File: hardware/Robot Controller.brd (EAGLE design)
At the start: 50.5 x 38.1 mm, 10 parts

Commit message: added a host pin
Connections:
- new net N$2: ATTINY.15, JP1.11
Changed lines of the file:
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@@
 <wire x1="81.2292" y1="76.2" x2="81.28" y2="76.2" width="0.254" layer="1"/>
+</signal>
+<signal name="N$2">
+<contactref element="JP1" pad="11"/>
+<contactref element="ATTINY" pad="15"/>
+<wire x1="71.755" y1="55.88" x2="81.28" y2="63.5" width="0" layer="19" extent="1-1"/>
 </signal>
 </signals>

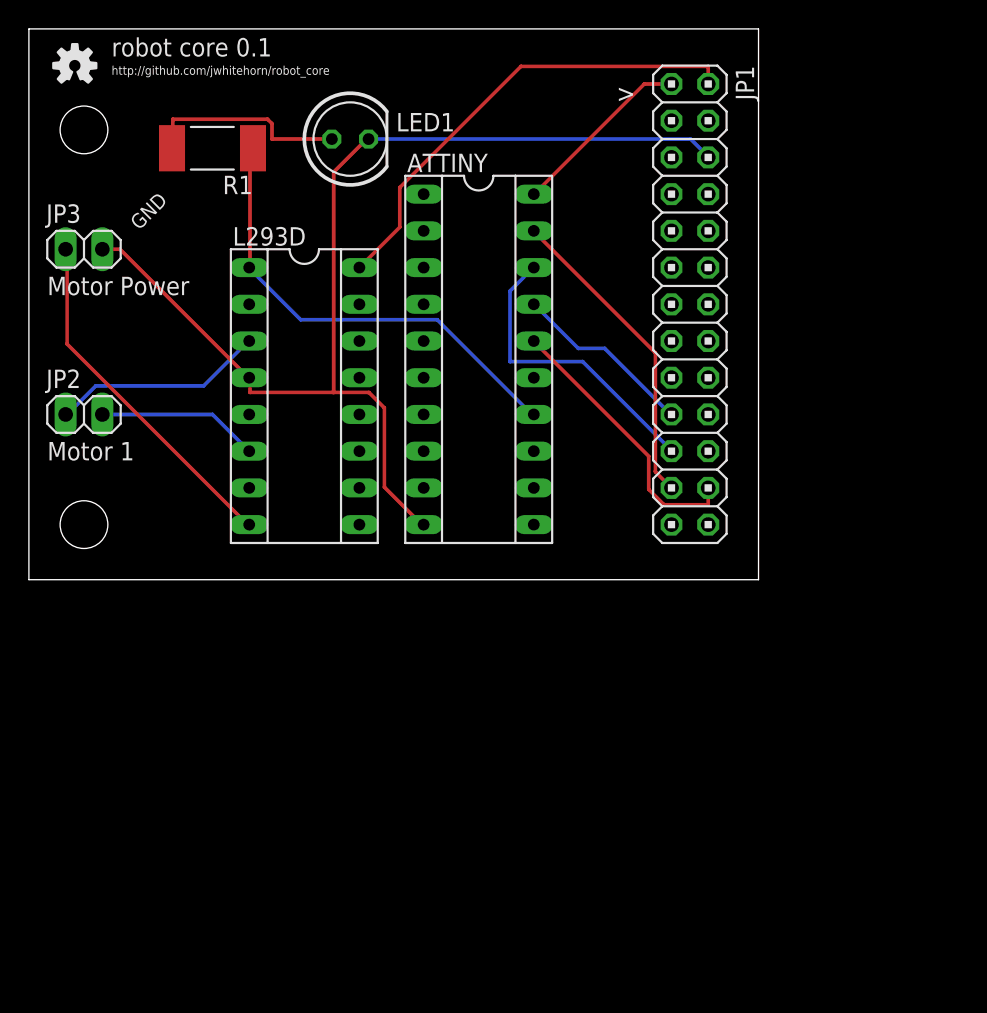
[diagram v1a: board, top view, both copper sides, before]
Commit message: thinking out how motor direction will be controlled
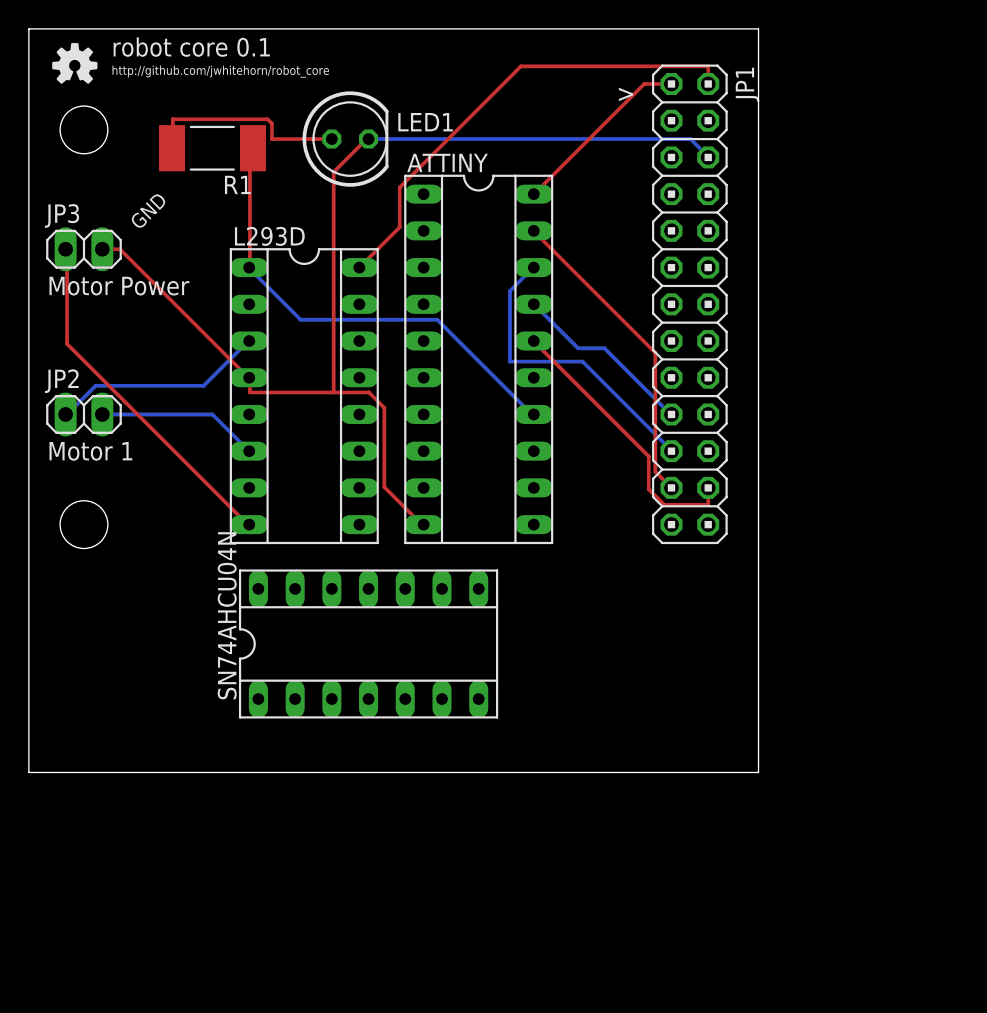
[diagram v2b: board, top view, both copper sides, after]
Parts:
- added SN74AHCU04N: (no value), ic-package:SOCKET-14
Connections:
- new net N$13: ATTINY.4, L293D.7, SN74AHCU04N.13
- new net N$15: L293D.2, SN74AHCU04N.12
- net GND: now also L293D.12, L293D.13, L293D.5, SN74AHCU04N.7
- net VCC: now also SN74AHCU04N.14
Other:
- board size 50.5 x 38.1 mm -> 50.5 x 51.4 mm
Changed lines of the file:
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@@
 <board>
 <plain>
-<wire x1="36.83" y1="41.91" x2="87.3" y2="41.91" width="0" layer="20"/>
-<wire x1="87.3" y1="41.91" x2="87.3" y2="80" width="0" layer="20"/>
-<wire x1="36.83" y1="80" x2="36.83" y2="41.91" width="0" layer="20"/>
+<wire x1="36.83" y1="28.575" x2="87.3" y2="28.575" width="0" layer="20"/>
+<wire x1="87.3" y1="28.575" x2="87.3" y2="80" width="0" layer="20"/>
+<wire x1="36.83" y1="80" x2="36.83" y2="28.575" width="0" layer="20"/>
 <text x="44.45" y="66.04" size="1.016" layer="21" rot="R45">GND</text>
 <text x="38.1" y="61.595" size="1.27" layer="21">Motor Power</text>
@@
 <element name="LED1" library="led" package="LED5MM" value="" x="59.055" y="72.39"/>
 <element name="U$4" library="SparkFun-Aesthetics" package="OSHW-LOGO-S" value="" x="40.005" y="77.47"/>
+<element name="SN74AHCU04N" library="ic-package" package="SOCKET-14" value="" x="60.325" y="37.465"/>
 </elements>
 <signals>
@@
 <wire x1="83.82" y1="71.1708" x2="83.82" y2="71.12" width="0.254" layer="16"/>
 <wire x1="60.3504" y1="72.39" x2="60.325" y2="72.39" width="0.254" layer="16"/>
+<contactref element="L293D" pad="13"/>
+<contactref element="L293D" pad="12"/>
+<contactref element="L293D" pad="5"/>
+<contactref element="SN74AHCU04N" pad="7"/>
+<wire x1="60.3504" y1="54.864" x2="59.69" y2="55.88" width="0" layer="19" extent="1-1"/>
+<wire x1="52.07" y1="53.34" x2="52.1208" y2="54.864" width="0" layer="19" extent="1-1"/>
+<wire x1="59.69" y1="53.34" x2="60.3504" y2="54.864" width="0" layer="19" extent="1-1"/>
+<wire x1="67.945" y1="33.655" x2="64.008" y2="45.72" width="0" layer="19" extent="1-1"/>
 </signal>
 <signal name="VCC">
@@
 <wire x1="71.7804" y1="68.58" x2="71.755" y2="68.58" width="0.254" layer="1"/>
 <wire x1="81.2292" y1="76.2" x2="81.28" y2="76.2" width="0.254" layer="1"/>
+<contactref element="SN74AHCU04N" pad="14"/>
+<wire x1="52.705" y1="41.275" x2="71.7804" y2="68.58" width="0" layer="19" extent="1-1"/>
 </signal>
 <signal name="N$2">
@@
 <wire x1="71.755" y1="55.88" x2="81.28" y2="63.5" width="0" layer="19" extent="1-1"/>
 </signal>
+<signal name="N$13">
+<contactref element="ATTINY" pad="4"/>
+<contactref element="SN74AHCU04N" pad="13"/>
+<contactref element="L293D" pad="7"/>
+<wire x1="52.07" y1="48.26" x2="64.135" y2="60.96" width="0" layer="19" extent="1-1"/>
+<wire x1="55.245" y1="41.275" x2="52.07" y2="48.26" width="0" layer="19" extent="1-1"/>
+</signal>
+<signal name="N$15">
+<contactref element="L293D" pad="2"/>
+<contactref element="SN74AHCU04N" pad="12"/>
+<wire x1="57.785" y1="41.275" x2="52.07" y2="60.96" width="0" layer="19" extent="1-1"/>
+</signal>
 </signals>

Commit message: tweak hardware design
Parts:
- removed JP2: Motor 1, pinhead:1X02
- removed JP3: Motor Power, pinhead:1X02
- removed U$1, U$2: (no value), SparkFun-Electromechanical:STAND-OFF
- removed U$4: (no value), SparkFun-Aesthetics:OSHW-LOGO-S
- added H1, H2: MOUNT-HOLE2.8, holes:2,8
- added LED2: (no value), led:1206
- added R2: (no value), resistor:R3216
- added SL1, SL2: (no value), con-amp-quick:02P
- LED1: device led:LED5MM -> led:1206
- R1: device resistor:R6332 -> resistor:R3216
- moved L293D 35.3 mm to (77.5, 26.7), turned to 0 degrees
- moved R1 31.0 mm to (74.9, 54.0), turned to 0 degrees
- moved LED1 28.5 mm to (85.7, 62.2), turned to 180 degrees
- moved JP1 18.4 mm to (95.9, 48.3)
- moved ATTINY 18.3 mm to (83.2, 47.0)
- moved SN74AHCU04N 12.8 mm to (71.8, 43.2), turned to 270 degrees
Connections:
- removed net N$11: LED1.A, R1.2
- new net N$16: ATTINY.2, R2.1
- new net N$17: LED2.A, R2.2
- new net N$3: LED1.A, R1.1
- net GND: now also LED1.C, LED2.C, SL2.2; no longer JP3.2, LED1.K
- net N$1: now also R1.2; no longer R1.1
- net N$10: now also SL2.1; no longer JP3.1
- net N$8: now also SL1.2; no longer JP2.1
- net N$9: now also SL1.1; no longer JP2.2
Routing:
- net N$10: track 24.4 -> 64.7 mm
- net N$8: track 14.8 -> 51.6 mm, vias 0 -> 1
- net N$13: track 0.00 -> 35.5 mm, vias 0 -> 1
- net N$9: track 11.2 -> 44.6 mm
- net GND: track 76.5 -> 108.7 mm
- net N$12: track 32.7 -> 58.3 mm
- net N$15: track 0.00 -> 24.8 mm
- net N$17: track 0.00 -> 23.7 mm
- net N$1: track 32.3 -> 52.1 mm, vias 0 -> 1
- net N$3: track 0.00 -> 17.5 mm, vias 0 -> 2
- net N$16: track 0.00 -> 17.0 mm
- net VCC: track 12.7 -> 28.1 mm
- net N$11: track 14.2 -> 0.00 mm
- net N$2: track 0.00 -> 9.79 mm
- net N$5: track 12.7 -> 18.1 mm
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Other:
- board size 50.5 x 51.4 mm -> 37.8 x 48.2 mm
- board text added: "robot core"
- board text removed: "GND"
- board text removed: "http://github.com/jwhitehorn/robot_core"
- board text removed: "robot core 0.1"

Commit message: change host pin
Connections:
- net N$2: now also ATTINY.3; no longer ATTINY.15
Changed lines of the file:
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@@
 <signal name="N$2">
 <contactref element="JP1" pad="11"/>
-<contactref element="ATTINY" pad="15"/>
 <wire x1="89.916" y1="48.6156" x2="87.0204" y2="45.72" width="0.254" layer="16"/>
 <wire x1="92.5068" y1="48.6156" x2="89.916" y2="48.6156" width="0.254" layer="16"/>
 <wire x1="94.6404" y1="50.7492" x2="92.5068" y2="48.6156" width="0.254" layer="16"/>
-<wire x1="87.0204" y1="45.72" x2="86.995" y2="45.72" width="0.254" layer="16"/>
 <wire x1="94.6404" y1="50.7492" x2="94.615" y2="50.8" width="0.254" layer="16"/>
+<contactref element="ATTINY" pad="3"/>
+<wire x1="79.375" y1="53.34" x2="87.0204" y2="45.72" width="0" layer="19" extent="16-16"/>
 </signal>
 <signal name="N$13">

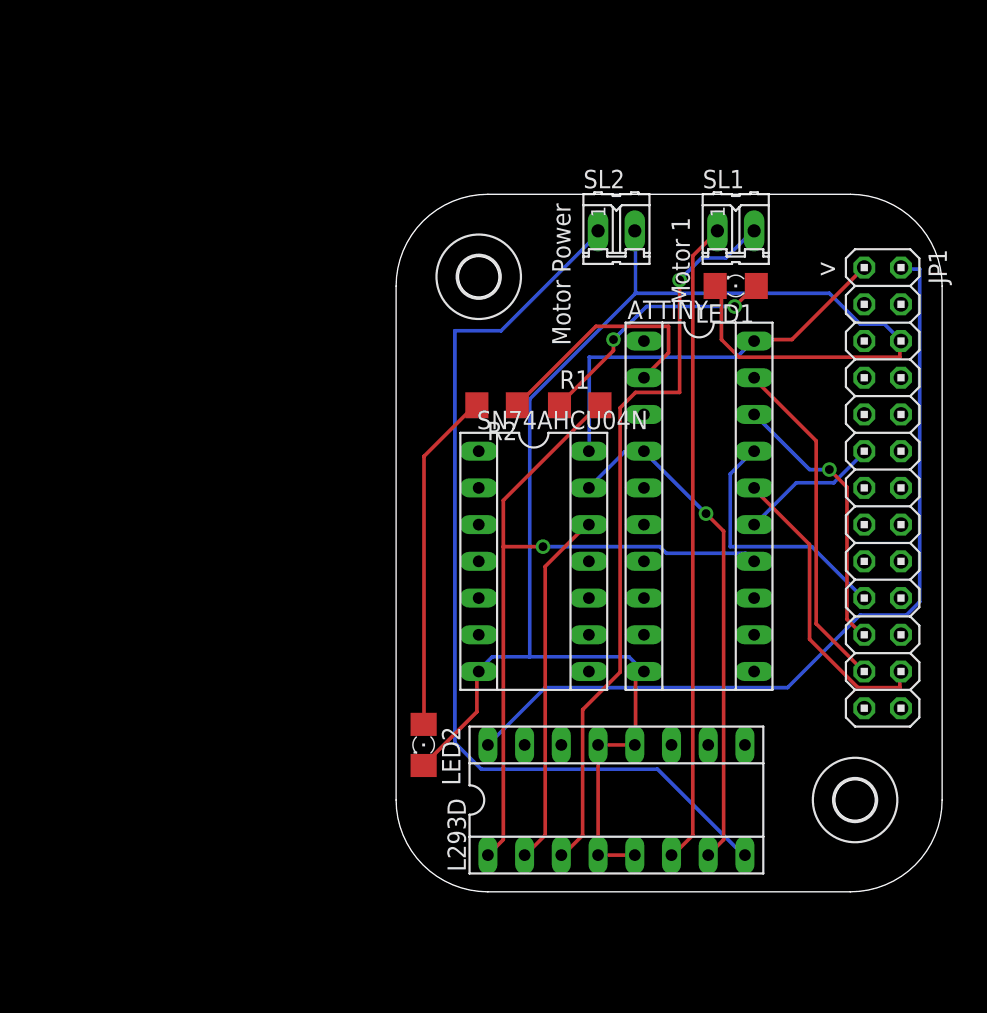
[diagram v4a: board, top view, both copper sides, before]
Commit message: update hardware for second motor
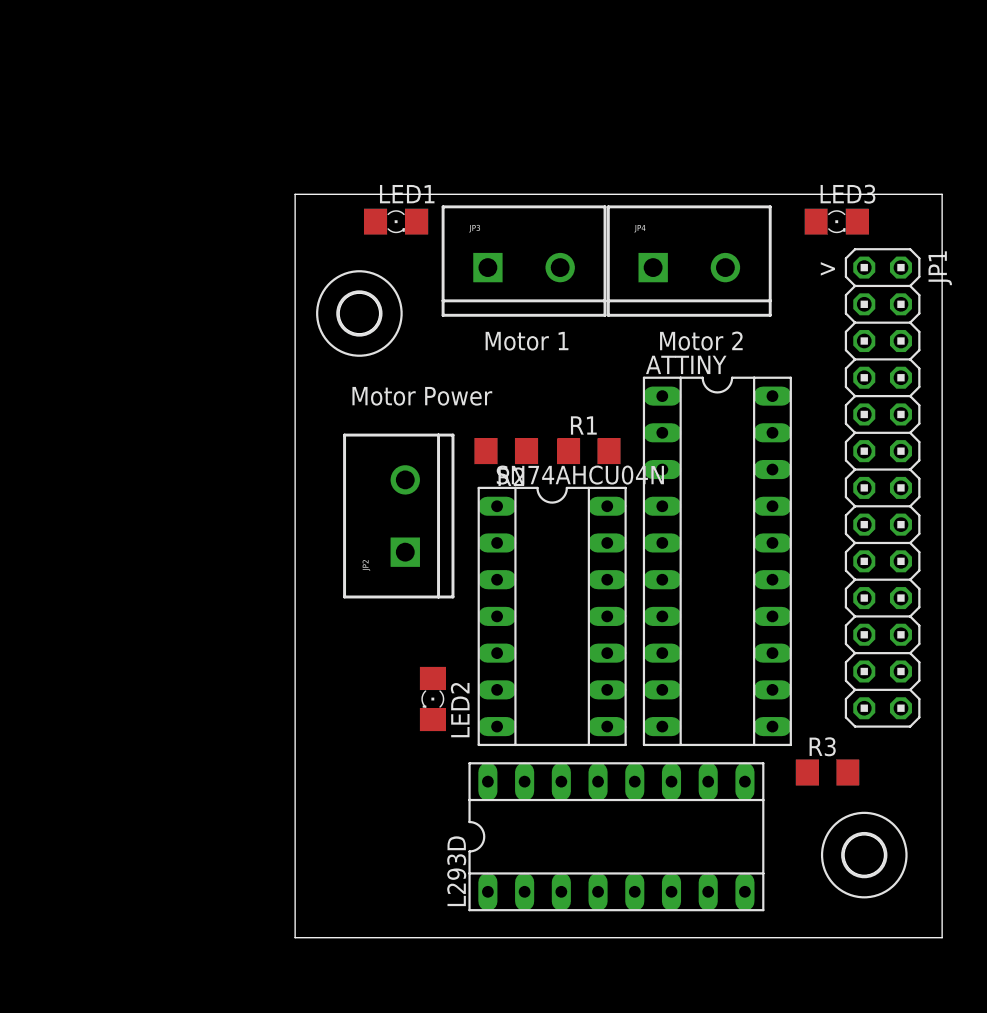
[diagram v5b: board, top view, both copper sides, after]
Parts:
- removed SL1, SL2: (no value), con-amp-quick:02P
- added JP2, JP3, JP4: (no value), SparkFun-Connectors:SCREWTERMINAL-5MM-2
- added LED3: (no value), led:1206
- added R3: (no value), resistor:R3216
- moved LED1 23.9 mm to (62.2, 66.7), turned to 0 degrees
- moved H1 8.64 mm to (59.7, 60.3)
- moved SN74AHCU04N 4.02 mm to (73.0, 39.4)
- moved ATTINY 4.02 mm to (84.5, 43.2)
- moved H2 3.86 mm to (94.6, 22.9)
- moved R1 3.24 mm to (75.6, 50.8)
- moved R2 3.24 mm to (69.8, 50.8)
- moved LED2 3.24 mm to (64.8, 33.7)
- moved L293D 2.54 mm to (77.5, 24.1)
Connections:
- new net N$11: ATTINY.15, L293D.9, R3.2
- new net N$14: LED3.A, R3.1
- new net N$18: JP4.1, L293D.14
- new net N$19: JP4.2, L293D.11
- net GND: now also JP3.2, LED3.C; no longer SL2.2
- net N$10: now also JP3.1; no longer SL2.1
- net N$8: now also JP2.2; no longer SL1.2
- net N$9: now also JP2.1; no longer SL1.1
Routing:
- net GND: track 108.7 -> 0.00 mm
- net N$10: track 64.7 -> 0.00 mm
- net N$12: track 58.3 -> 0.00 mm
- net N$1: track 52.1 -> 0.00 mm, vias 1 -> 0
- net N$8: track 51.6 -> 0.00 mm, vias 1 -> 0
- net N$9: track 44.6 -> 0.00 mm
- net N$13: track 35.5 -> 0.00 mm, vias 1 -> 0
- net VCC: track 28.1 -> 0.00 mm
- net N$15: track 24.8 -> 0.00 mm
- net N$17: track 23.7 -> 0.00 mm
- net N$7: track 23.5 -> 0.00 mm
- net N$4: track 20.8 -> 0.00 mm
- net N$6: track 19.3 -> 0.00 mm, vias 1 -> 0
- net N$5: track 18.1 -> 0.00 mm
- net N$3: track 17.5 -> 0.00 mm, vias 2 -> 0
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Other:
- board size 37.8 x 48.2 mm -> 44.8 x 51.4 mm
- board text added: "Motor 2"

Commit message: ideas around master/slave robot cores
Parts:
- added JP5, JP6: (no value), pinhead:1X07
- moved H2 48.4 mm to (46.4, 19.7)
- moved R3 38.8 mm to (62.2, 53.3)
- moved JP4 13.4 mm to (66.7, 62.2)
- moved SN74AHCU04N 13.4 mm to (59.7, 38.1)
- moved H1 13.4 mm to (46.4, 59.1)
- moved JP2 13.4 mm to (49.5, 42.5)
- moved JP3 13.4 mm to (55.2, 62.2)
- moved R1 13.4 mm to (62.2, 49.5)
- moved ATTINY 13.4 mm to (71.1, 41.9)
- moved LED2 13.4 mm to (51.4, 32.4)
- moved LED1 13.4 mm to (48.9, 65.4)
- moved LED3 13.4 mm to (79.4, 65.4)
- moved R2 13.4 mm to (56.5, 49.5)
- moved L293D 12.8 mm to (64.8, 22.9)
- moved JP1 9.16 mm to (90.8, 40.6)
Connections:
- net GND: now also JP5.6
- net N$12: now also JP5.1
- net N$4: now also JP5.2
- net N$5: now also JP5.4
- net N$7: now also JP5.3
- net VCC: now also JP5.7
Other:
- board size 44.8 x 51.4 mm -> 52.4 x 52.7 mm
- board text added: "master core"
- board text added: "slave core"

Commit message: WIP dev board
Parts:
- removed H2: MOUNT-HOLE2.8, holes:2,8
- added JP8: (no value), pinhead:1X10
- added S1: (no value), switch-omron:B3F-10XX
- JP6: device pinhead:1X07 -> pinhead:1X03
- moved L293D 23.3 mm to (81.3, 39.4), turned to 270 degrees
- moved R1 17.3 mm to (79.4, 52.1)
- moved LED2 8.28 mm to (47.0, 25.4)
- moved JP6 6.25 mm to (79.4, 58.4), turned to 90 degrees
- moved JP5 3.17 mm to (85.1, 21.0)
- moved JP2 2.54 mm to (47.0, 42.5)
- moved SN74AHCU04N 2.54 mm to (57.1, 38.1)
- moved ATTINY 1.91 mm to (69.2, 41.9)
- moved R2 1.42 mm to (55.2, 50.2), turned to 0 degrees
- moved R3 1.42 mm to (61.0, 52.7), turned to 90 degrees
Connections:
- new net N$20: ATTINY.5, L293D.10, SN74AHCU04N.11
- new net N$21: JP6.1, R2.1
- new net N$22: L293D.15, SN74AHCU04N.10
- new net N$23: JP6.3, JP8.8
- new net N$24: ATTINY.6, JP8.7
- new net N$25: ATTINY.7, JP8.6
- new net N$26: ATTINY.8, JP8.5
- new net N$27: ATTINY.9, JP8.4
- new net N$28: ATTINY.13, JP8.1
- new net N$29: ATTINY.12, JP8.2
- new net N$30: ATTINY.11, JP8.3
- new net N$31: ATTINY.1, S1.3
- net GND: now also JP8.10, S1.2
- net N$16: now also JP6.2; no longer R2.1
- net VCC: now also JP8.9
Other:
- board size 52.4 x 52.7 mm -> 52.4 x 48.9 mm
- board text removed: "master core"
- board text removed: "slave core"

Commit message: silkscreen work
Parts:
- moved JP6 32.5 mm to (47.0, 55.9), turned to 180 degrees
- moved R1 15.5 mm to (88.3, 64.8)
- moved LED1 14.1 mm to (60.3, 57.1)
- moved LED3 10.8 mm to (72.4, 57.1)
- moved S1 9.53 mm to (81.3, 54.6), turned to 180 degrees
- moved LED2 7.01 mm to (47.6, 32.4)
- moved R3 6.38 mm to (54.6, 53.3), turned to 180 degrees
- moved JP1 5.08 mm to (90.8, 45.7)
- moved JP5 3.81 mm to (81.3, 21.0)
- moved JP8 3.81 mm to (59.7, 21.0)
- moved H1 3.24 mm to (47.0, 62.2)
- moved JP4 2.62 mm to (69.2, 62.9)
- moved JP3 0.90 mm to (55.9, 62.9)
- moved R2 0.90 mm to (54.6, 49.5), turned to 180 degrees
- moved JP2 0.64 mm to (46.4, 42.5)
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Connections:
- net N$6: now also JP5.5
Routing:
- net GND: track 0.00 -> 156.3 mm, vias 0 -> 1
- net VCC: track 0.00 -> 80.3 mm
- net N$10: track 0.00 -> 73.0 mm, vias 0 -> 1
- net N$22: track 0.00 -> 64.3 mm
- net N$11: track 0.00 -> 55.7 mm, vias 0 -> 3
- net N$23: track 0.00 -> 51.7 mm
- net N$7: track 0.00 -> 50.5 mm, vias 0 -> 1
- net N$20: track 0.00 -> 48.2 mm, vias 0 -> 1
- net N$4: track 0.00 -> 46.9 mm, vias 0 -> 1
- net N$12: track 0.00 -> 46.7 mm
- net N$6: track 0.00 -> 45.7 mm
- net N$5: track 0.00 -> 40.8 mm, vias 0 -> 2
- net N$1: track 0.00 -> 39.2 mm, vias 0 -> 2
- net N$19: track 0.00 -> 37.1 mm
- net N$8: track 0.00 -> 36.7 mm
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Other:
- outline, holes or cut-outs redrawn
- board text added: "3V3"
- board text added: "5V"
- board text added: "GND"
- board text added: "M-PWR"
- board text added: "M1"
- board text added: "M2"
- board text added: "MISO"
- board text added: "MOSI"
- board text added: "PB0"
- board text added: "PB1"
- board text added: "PD0"
- board text added: "PD2"
- board text added: "PD3"
- board text added: "PD4"
- board text added: "PD5"
- board text added: "PD6"
- board text added: "SCLK"
- board text added: "SS"
- board text removed: "Motor 1"
- board text removed: "Motor 2"
- board text removed: "Motor Power"
